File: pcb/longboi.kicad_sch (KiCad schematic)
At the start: 32 parts, among them J1 Testpad, J2 Testpad, J3 Testpad, J4 Testpad, J5 Testpad, J6 JST-PH, U1 STM32H723VGTx, Y1 25MHz

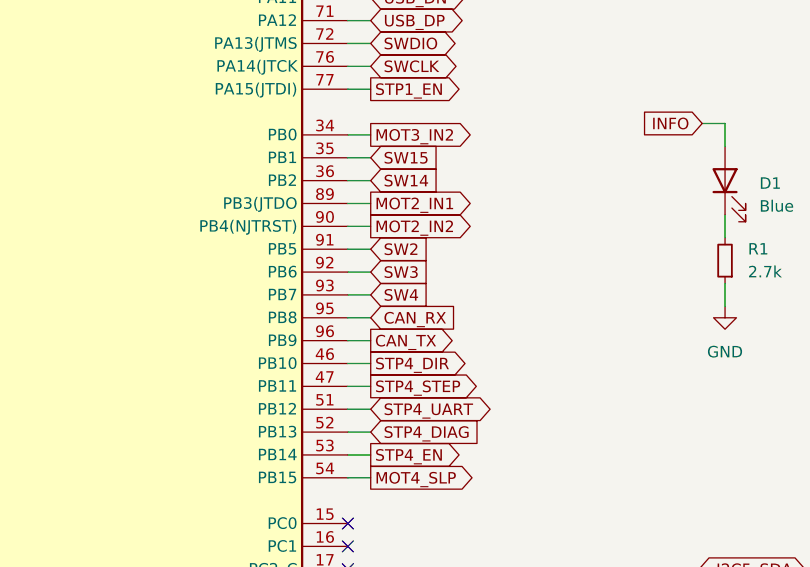
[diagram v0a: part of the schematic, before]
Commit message: fixes #18 fixes #26
replace usb-c connector
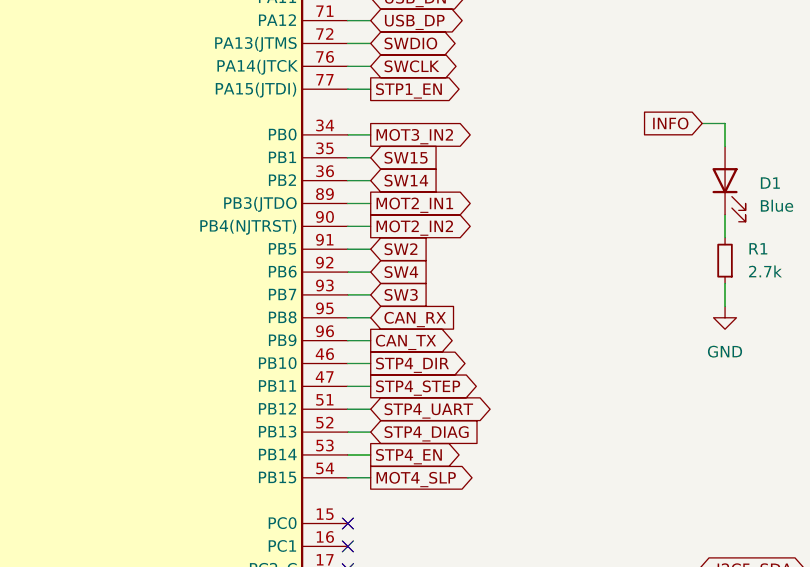
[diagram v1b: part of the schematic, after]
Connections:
- net SW3: now also U1.93 (PB7); no longer U1.92 (PB6)
- net SW4: now also U1.92 (PB6); no longer U1.93 (PB7)
